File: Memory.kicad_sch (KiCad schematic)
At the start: 11 parts, among them U10 SST39SF040, U11 SST39SF040, U7 AS6C4008-55PCN, U8 AS6C4008-55PCN

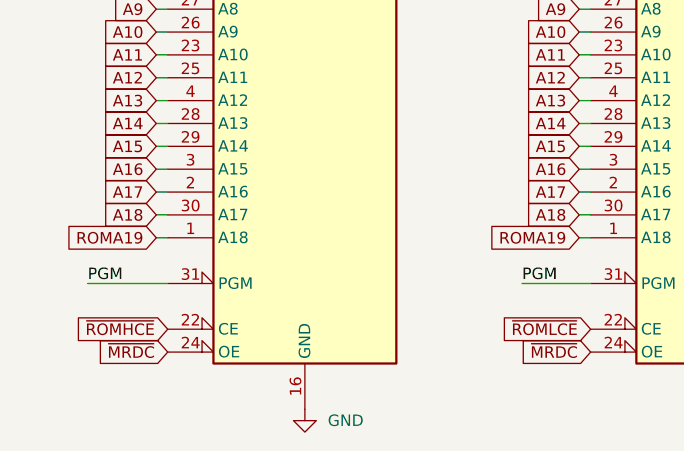
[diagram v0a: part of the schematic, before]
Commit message: Adjusted Data Bus for 80130
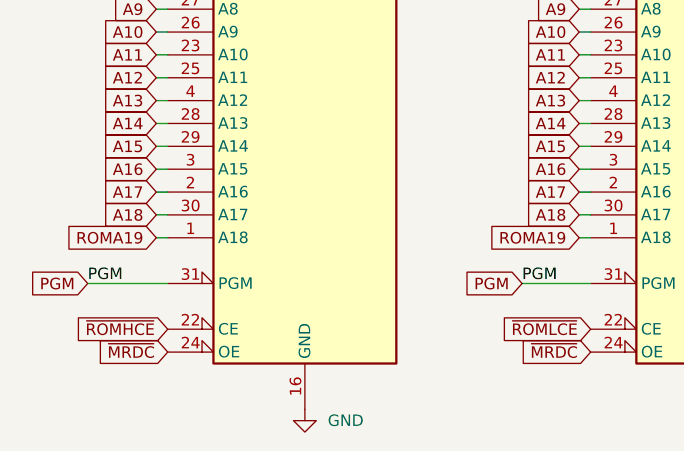
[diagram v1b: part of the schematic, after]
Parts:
- U10, U11: footprint (none) -> Package_DIP:DIP-32_W15.24mm
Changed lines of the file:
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@@
+		)
+	)
+	(global_label "PGM"
+		(shape input)
+		(at 76.2 162.56 180)
+		(fields_autoplaced yes)
+		(effects
+			(font
+				(size 1.27 1.27)
+			)
+			(justify right)
+		)
+		(property "Intersheetrefs" "${INTERSHEET_REFS}"
+			(at 69.2234 162.56 0)
+			(effects
+				(font
+					(size 1.27 1.27)
+				)
+				(justify right)
+				(hide yes)
+			)
 		)
 	)
@@
 				)
 				(justify left)
+				(hide yes)
+			)
+		)
+	)
+	(global_label "PGM"
+		(shape input)
+		(at 27.94 162.56 180)
+		(fields_autoplaced yes)
+		(effects
+			(font
+				(size 1.27 1.27)
+			)
+			(justify right)
+		)
+		(property "Intersheetrefs" "${INTERSHEET_REFS}"
+			(at 20.9634 162.56 0)
+			(effects
+				(font
+					(size 1.27 1.27)
+				)
+				(justify right)
 				(hide yes)
 			)
@@
 			)
 		)
-		(property "Footprint" ""
+		(property "Footprint" "Package_DIP:DIP-32_W15.24mm"
 			(at 99.06 134.62 0)
 			(effects
@@
 			)
 		)
-		(property "Footprint" ""
+		(property "Footprint" "Package_DIP:DIP-32_W15.24mm"
 			(at 52.07 134.62 0)
 			(effects

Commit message: assigned all footprints
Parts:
- C5, C7, C8, C9: footprint (none) -> Capacitor_THT:C_Disc_D8.0mm_W2.5mm_P5.00mm
- C6: footprint (none) -> Capacitor_THT:CP_Radial_D5.0mm_P2.50mm
- JP1: footprint (none) -> Connector_PinHeader_2.54mm:PinHeader_1x02_P2.54mm_Vertical
- R8: footprint (none) -> Resistor_THT:R_Axial_DIN0207_L6.3mm_D2.5mm_P7.62mm_Horizontal
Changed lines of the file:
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@@
 			)
 		)
-		(property "Footprint" ""
+		(property "Footprint" "Capacitor_THT:C_Disc_D8.0mm_W2.5mm_P5.00mm"
 			(at 148.2852 105.41 0)
 			(effects
@@
 			)
 		)
-		(property "Footprint" ""
+		(property "Footprint" "Capacitor_THT:C_Disc_D8.0mm_W2.5mm_P5.00mm"
 			(at 173.6852 105.41 0)
 			(effects
@@
 			)
 		)
-		(property "Footprint" ""
+		(property "Footprint" "Capacitor_THT:CP_Radial_D5.0mm_P2.50mm"
 			(at 196.85 101.6 0)
 			(effects
@@
 			)
 		)
-		(property "Footprint" ""
+		(property "Footprint" "Capacitor_THT:C_Disc_D8.0mm_W2.5mm_P5.00mm"
 			(at 160.9852 105.41 0)
 			(effects
@@
 			)
 		)
-		(property "Footprint" ""
+		(property "Footprint" "Resistor_THT:R_Axial_DIN0207_L6.3mm_D2.5mm_P7.62mm_Horizontal"
 			(at 170.942 66.04 90)
 			(effects
@@
 			)
 		)
-		(property "Footprint" ""
+		(property "Footprint" "Capacitor_THT:C_Disc_D8.0mm_W2.5mm_P5.00mm"
 			(at 185.1152 105.41 0)
 			(effects
@@
 			)
 		)
-		(property "Footprint" ""
+		(property "Footprint" "Connector_PinHeader_2.54mm:PinHeader_1x02_P2.54mm_Vertical"
 			(at 160.02 62.23 0)
 			(effects
